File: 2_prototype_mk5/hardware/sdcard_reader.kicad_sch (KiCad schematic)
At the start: 4 parts, among them J1 Micro_SD_Card

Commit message: Successful MKV software test (after minor modification)
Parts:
- C5: LCSC_Part_Number C13585 -> C77093
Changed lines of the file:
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@@
 			)
 		)
-		(property "LCSC_Part_Number" "C13585"
+		(property "LCSC_Part_Number" "C77093"
 			(at 97.79 60.96 0)
 			(hide yes)

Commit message: MKV revision 1
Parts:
- C5: LCSC Part Number (none) -> C14860; LCSC_Part_Number C77093 -> (none)
- C6: LCSC Part Number (none) -> C14663; LCSC_Part_Number C14663 -> (none)
- J1: LCSC Part Number (none) -> C719027; LCSC_Part_Number C719027 -> (none)
- RN1: LCSC Part Number (none) -> C779384; LCSC_Part_Number C779384 -> (none)
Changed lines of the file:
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@@
-			)
-		)
-		(property "LCSC_Part_Number" "C779384"
-			(at 88.9 77.47 0)
-			(hide yes)
-			(show_name no)
-			(do_not_autoplace no)
-			(effects
-				(font
-					(size 1.27 1.27)
-				)
 			)
 		)
@@
 		)
 		(property "SnapEDA_Link" ""
+			(at 88.9 77.47 0)
+			(hide yes)
+			(show_name no)
+			(do_not_autoplace no)
+			(effects
+				(font
+					(size 1.27 1.27)
+				)
+			)
+		)
+		(property "LCSC Part Number" "C779384"
 			(at 88.9 77.47 0)
 			(hide yes)
@@
 			)
 		)
-		(property "LCSC_Part_Number" "C14663"
-			(at 113.03 60.96 0)
-			(hide yes)
-			(show_name no)
-			(do_not_autoplace no)
-			(effects
-				(font
-					(size 1.27 1.27)
-				)
-			)
-		)
 		(property "Availability" ""
 			(at 113.03 60.96 0)
@@
 		)
 		(property "SnapEDA_Link" ""
+			(at 113.03 60.96 0)
+			(hide yes)
+			(show_name no)
+			(do_not_autoplace no)
+			(effects
+				(font
+					(size 1.27 1.27)
+				)
+			)
+		)
+		(property "LCSC Part Number" "C14663"
 			(at 113.03 60.96 0)
 			(hide yes)
@@
 			)
 		)
-		(property "LCSC_Part_Number" "C719027"
-			(at 147.32 92.71 0)
-			(hide yes)
-			(show_name no)
-			(do_not_autoplace no)
-			(effects
-				(font
-					(size 1.27 1.27)
-				)
-			)
-		)
 		(property "Availability" ""
 			(at 147.32 92.71 0)
@@
 		)
 		(property "SnapEDA_Link" ""
+			(at 147.32 92.71 0)
+			(hide yes)
+			(show_name no)
+			(do_not_autoplace no)
+			(effects
+				(font
+					(size 1.27 1.27)
+				)
+			)
+		)
+		(property "LCSC Part Number" "C719027"
 			(at 147.32 92.71 0)
 			(hide yes)
@@
 			)
 		)
-		(property "LCSC_Part_Number" "C77093"
-			(at 97.79 60.96 0)
-			(hide yes)
-			(show_name no)
-			(do_not_autoplace no)
-			(effects
-				(font
-					(size 1.27 1.27)
-				)
-			)
-		)
 		(property "Availability" ""
 			(at 97.79 60.96 0)
@@
 			(at 97.79 60.96 0)
 			(hide yes)
+			(show_name no)
+			(do_not_autoplace no)
+			(effects
+				(font
+					(size 1.27 1.27)
+				)
+			)
+		)
+		(property "LCSC Part Number" "C14860"
+			(at 97.79 60.96 0)
+			(hide yes)

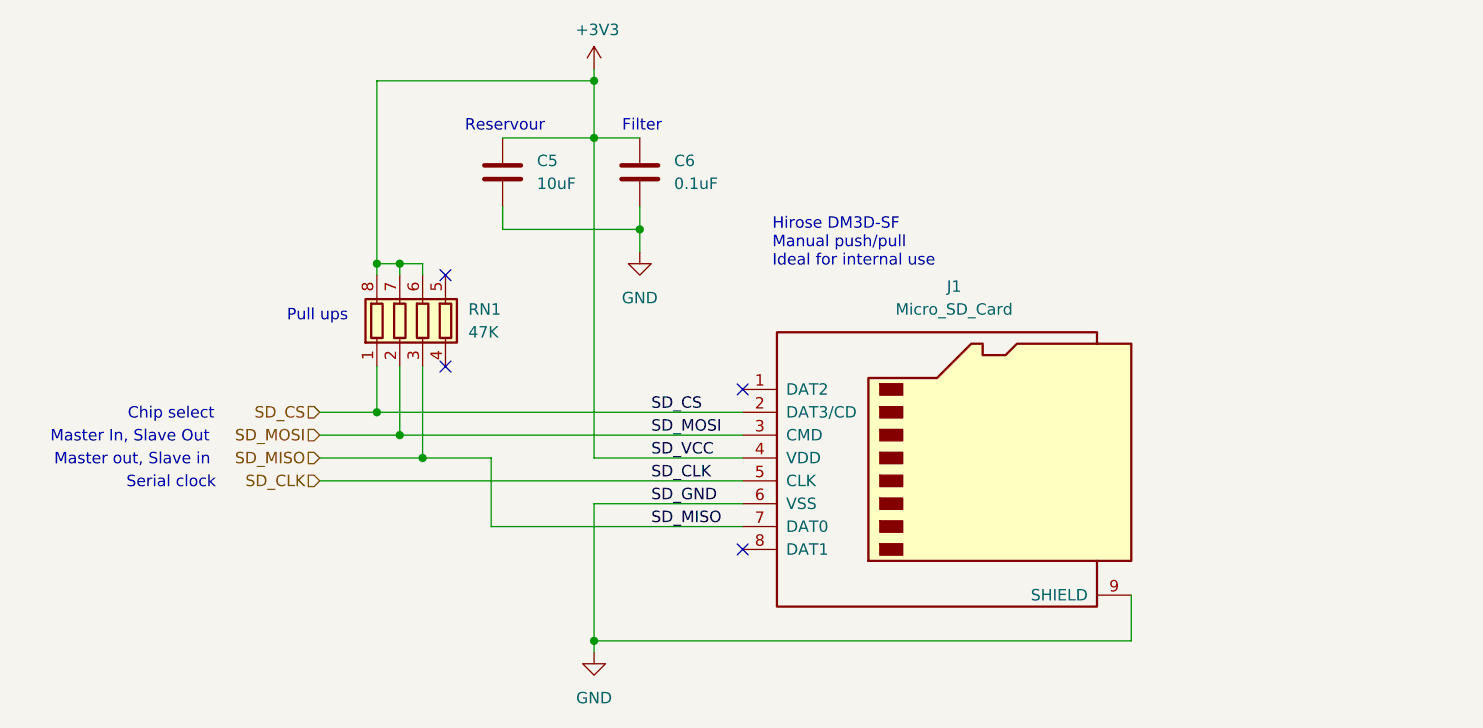
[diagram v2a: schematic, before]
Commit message: Cost reductions for JCLPCB
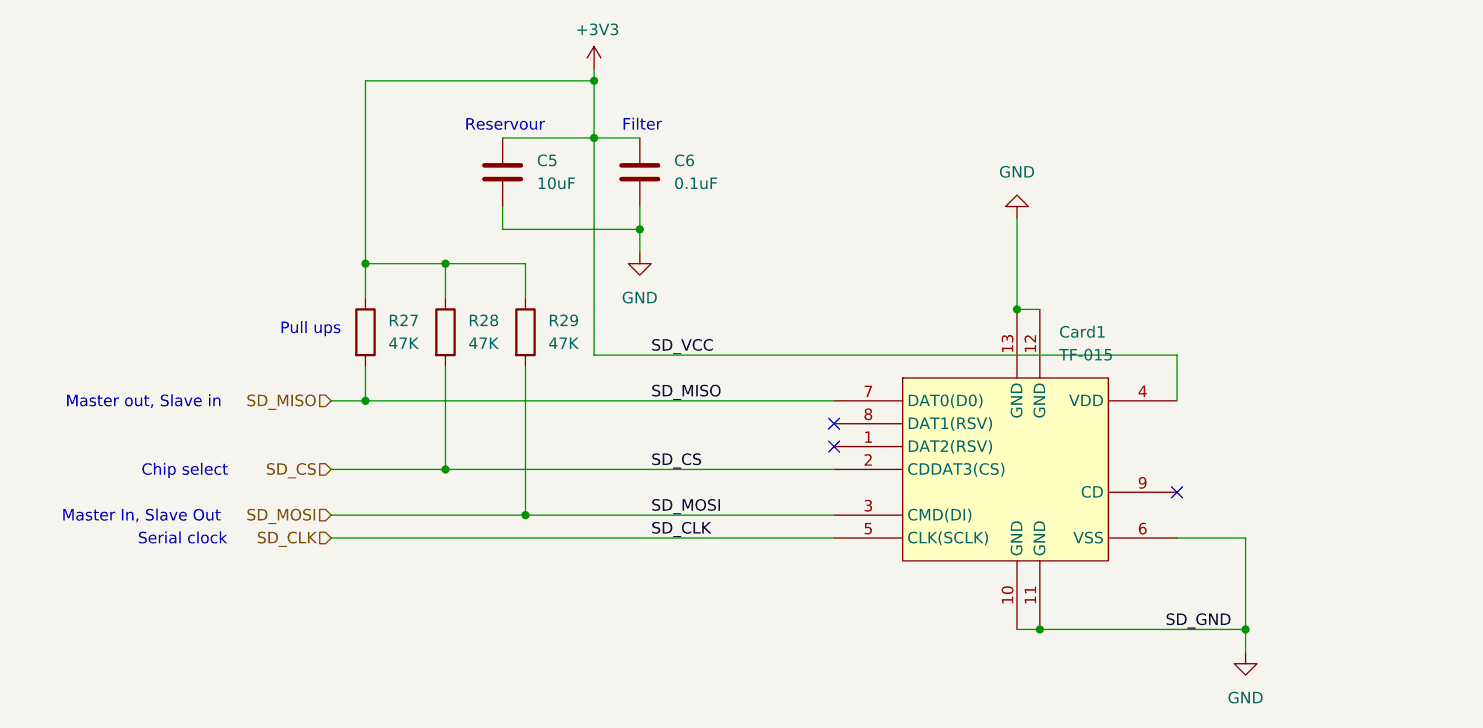
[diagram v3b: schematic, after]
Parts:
- removed J1: Micro_SD_Card, Connector_Card:microSD_HC_Hirose_DM3D-SF, symbol Connector:Micro_SD_Card
- removed RN1: 47K, Resistor_SMD:R_Array_Convex_4x0603, symbol Device:R_Pack04
- added Card1: TF-015, easyeda2kicad:TF-SMD_TF-015, symbol easyeda2kicad:TF-015
- added R27, R28, R29: 47K, Resistor_SMD:R_0402_1005Metric, symbol Device:R
- C5: LCSC Part Number C14860 -> C13585
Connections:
- net +3V3: now also Card1.4 (VDD), R27.1, R28.1, R29.1
- net GND: now also Card1.10 (GND), Card1.11 (GND), Card1.12 (GND), Card1.13 (GND), Card1.6 (VSS)
- net SD_CLK: now also Card1.5 (CLK(SCLK))
- net SD_CS: now also Card1.2 (CDDAT3(CS)), R28.2
- net SD_MISO: now also Card1.7 (DAT0(D0)), R27.2
- net SD_MOSI: now also Card1.3 (CMD(DI)), R29.2
- no-connect marks 4 -> 3
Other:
- note removed: "Hirose DM3D-SF Manual push/pull Ideal for internal use"

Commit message: Tweaks
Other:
- note added: "Stops ERC error"
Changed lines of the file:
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@@
 	(generator_version "10.0")
 	(paper "A4")
+	(text "Stops ERC error"
+		(exclude_from_sim no)
+		(at 195.326 101.092 0)
+		(effects
+			(font
+				(size 1.27 1.27)
+			)
+		)
+	)
 	(text "Master In, Slave Out"
 		(exclude_from_sim no)
@@
 		(pts
 			(xy 91.44 82.55) (xy 91.44 93.98)
+		)
+		(stroke
+			(width 0)
+			(type default)
+		)
+	)
+	(wire
+		(pts
+			(xy 195.58 109.22) (xy 195.58 111.76)
 		)
 		(stroke
@@
 					(size 1.27 1.27)
 					(italic yes)
+				)
+			)
+		)
+	)
+	(symbol
+		(lib_id "power:GND")
+		(at 195.58 111.76 0)
+		(unit 1)
+		(body_style 1)
+		(exclude_from_sim no)
+		(in_bom yes)
+		(on_board yes)
+		(in_pos_files yes)
+		(dnp no)
+		(fields_autoplaced yes)
+		(property "Reference" "#PWR017"
+			(at 195.58 118.11 0)
+			(hide yes)
+			(show_name no)
+			(do_not_autoplace no)
+			(effects
+				(font
+					(size 1.27 1.27)
+				)
+			)
+		)
+		(property "Value" "GND"
+			(at 195.58 116.84 0)
+			(show_name no)
+			(do_not_autoplace no)
+			(effects
+				(font
+					(size 1.27 1.27)
+				)
+			)
+		)
+		(property "Footprint" ""
+			(at 195.58 111.76 0)
+			(hide yes)
+			(show_name no)
+			(do_not_autoplace no)
+			(effects
+				(font
+					(size 1.27 1.27)
+				)
+			)
+		)
+		(property "Datasheet" ""
+			(at 195.58 111.76 0)
+			(hide yes)
+			(show_name no)
+			(do_not_autoplace no)
+			(effects
+				(font
+					(size 1.27 1.27)
+				)
+			)
+		)
+		(property "Description" "Power symbol creates a global label with name \"GND\" , ground"
+			(at 195.58 111.76 0)
+			(hide yes)
+			(show_name no)
+			(do_not_autoplace no)
+			(effects
+				(font
+					(size 1.27 1.27)
+				)
+			)
+		)
+		(pin "1"
+		)
+		(instances
+			(project "HDD Synth Prototype MK5"
+				(path "/1a22431a-ba36-40a0-9a7e-c2a82ec69c53/d1519e40-91bf-450d-a5bd-0730e6716e0a"
+					(reference "#PWR017")
+					(unit 1)
 				)
 			)
@@
 					(unit 1)
 				)
+			)
+		)
+	)
+	(symbol
+		(lib_id "power:PWR_FLAG")
+		(at 195.58 109.22 0)
+		(unit 1)
+		(body_style 1)
+		(exclude_from_sim no)
+		(in_bom yes)
+		(on_board yes)
+		(in_pos_files yes)
+		(dnp no)
+		(fields_autoplaced yes)
+		(property "Reference" "#FLG01"
+			(at 195.58 107.315 0)
+			(hide yes)
+			(show_name no)
+			(do_not_autoplace no)
+			(effects
+				(font
+					(size 1.27 1.27)
+				)
+			)
+		)
+		(property "Value" "PWR_FLAG"
+			(at 195.58 104.14 0)
+			(show_name no)
+			(do_not_autoplace no)
+			(effects
+				(font
+					(size 1.27 1.27)
+				)
+			)
+		)
+		(property "Footprint" ""
+			(at 195.58 109.22 0)
+			(hide yes)
+			(show_name no)
+			(do_not_autoplace no)
+			(effects
+				(font
+					(size 1.27 1.27)
+				)
+			)
+		)
+		(property "Datasheet" ""
+			(at 195.58 109.22 0)
+			(hide yes)
+			(show_name no)
+			(do_not_autoplace no)
+			(effects
+				(font
+					(size 1.27 1.27)
+				)
+			)
+		)
+		(property "Description" "Special symbol for telling ERC where power comes from"
+			(at 195.58 109.22 0)
+			(hide yes)
+			(show_name no)
+			(do_not_autoplace no)
+			(effects
+				(font
+					(size 1.27 1.27)
+				)
+			)
+		)
+		(pin "1"
+		)
+		(instances
+			(project "HDD Synth Prototype MK5"
+				(path "/1a22431a-ba36-40a0-9a7e-c2a82ec69c53/d1519e40-91bf-450d-a5bd-0730e6716e0a"
+					(reference "#FLG01")
+					(unit 1)
+				)

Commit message: 5.3.0 sent to JCLPCB
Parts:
- Card1: LCSC Part C113206 -> (none); LCSC Part Number (none) -> C113206
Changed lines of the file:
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@@
 			)
 		)
-		(property "LCSC Part" "C113206"
+		(property "LCSC Part" ""
 			(at 153.67 129.54 0)
 			(hide yes)
 			(show_name no)
+			(do_not_autoplace no)
+			(effects
+				(font
+					(size 1.27 1.27)
+				)
+			)
+		)
+		(property "LCSC Part Number" "C113206"
+			(at 153.67 93.98 0)
+			(hide yes)
+			(show_name no)
